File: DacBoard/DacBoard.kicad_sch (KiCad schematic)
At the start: 1 part

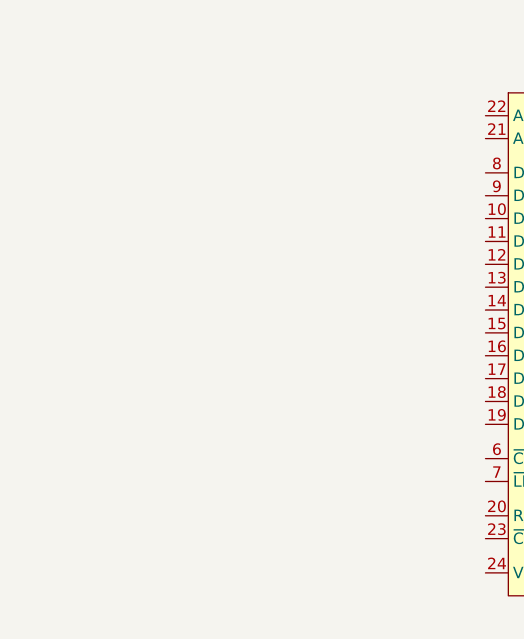
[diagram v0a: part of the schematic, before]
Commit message: Added a DAC board connector (PCIe 1x)
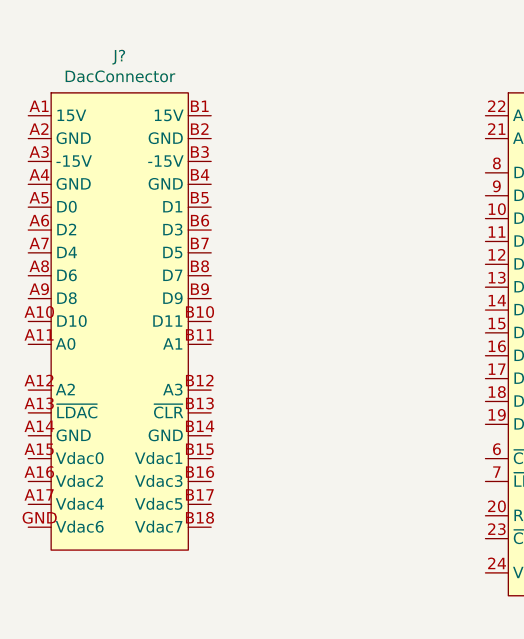
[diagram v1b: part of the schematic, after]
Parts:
- added J?: DacConnector, symbol Unichip:DacConnector
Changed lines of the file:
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@@
 (kicad_sch (version 20210126) (generator eeschema)
   (paper "A4")
+  (symbol (lib_id "Unichip:DacConnector") (at 86.36 50.8 0) (unit 1)
+    (in_bom yes) (on_board yes)
+    (property "Reference" "J?" (id 0) (at 86.36 46.7163 0))
+    (property "Value" "DacConnector" (id 1) (at 86.36 49.015 0))
+    (property "Footprint" "" (id 2) (at 86.36 50.8 0)
+      (effects (font (size 1.27 1.27)) hide)
+    )
+    (property "Datasheet" "" (id 3) (at 86.36 50.8 0)
+      (effects (font (size 1.27 1.27)) hide)
+    )
+    (pin "A1")
+    (pin "A2")
+    (pin "A3")
+    (pin "B1")
+    (pin "B2")
+    (pin "B3")
+    (pin "A4")
+    (pin "A5")
+    (pin "A6")
+    (pin "A7")
+    (pin "A8")
+    (pin "A9")
+    (pin "A10")
+    (pin "A11")
+    (pin "B6")
+    (pin "B7")
+    (pin "B8")
+    (pin "B9")
+    (pin "B10")
+    (pin "B11")
+    (pin "B4")
+    (pin "A12")
+    (pin "A13")
+    (pin "A14")
+    (pin "A15")
+    (pin "A16")
+    (pin "A17")
+    (pin "GND")
+    (pin "B12")
+    (pin "B14")
+    (pin "B15")
+    (pin "B13")
+    (pin "B16")
+    (pin "B17")
+    (pin "B18")
+    (pin "B5")
+  )
   (symbol (lib_id "Unichip:AD5725") (at 137.16 50.8 0) (unit 1)
     (in_bom yes) (on_board yes)
@@
   )
   (symbol_instances
+    (path "/40e80e6f-12f5-4eec-bb61-d86ec9cd78fd"
+      (reference "J?") (unit 1) (value "DacConnector") (footprint "")
+    )
     (path "/86d8534c-a77c-4bf0-ac2d-81d422c9a516"
       (reference "U?") (unit 1) (value "AD5725") (footprint "")

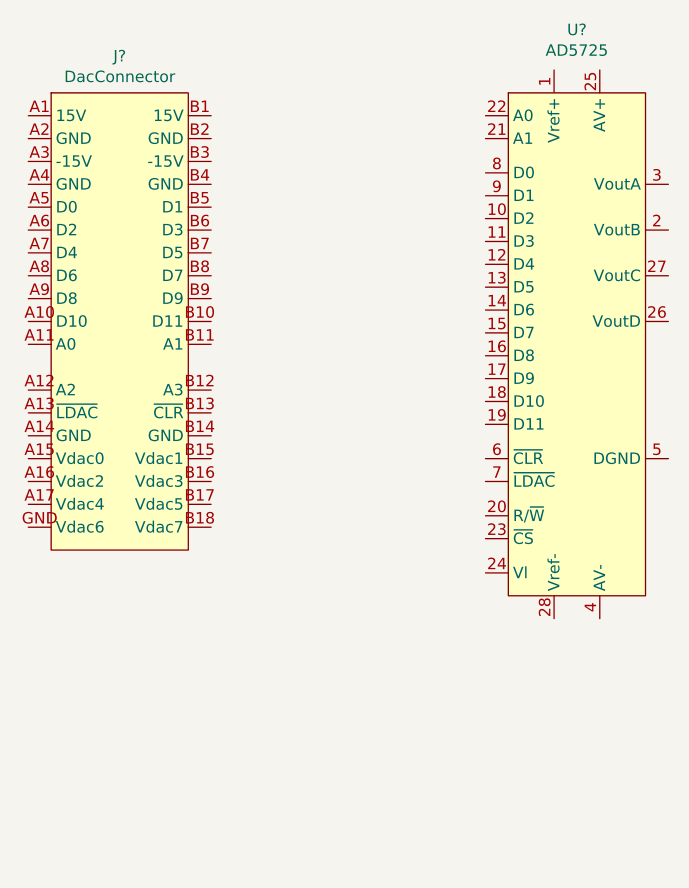
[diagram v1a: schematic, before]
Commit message: Changed DacConnector to be PCIe 4x
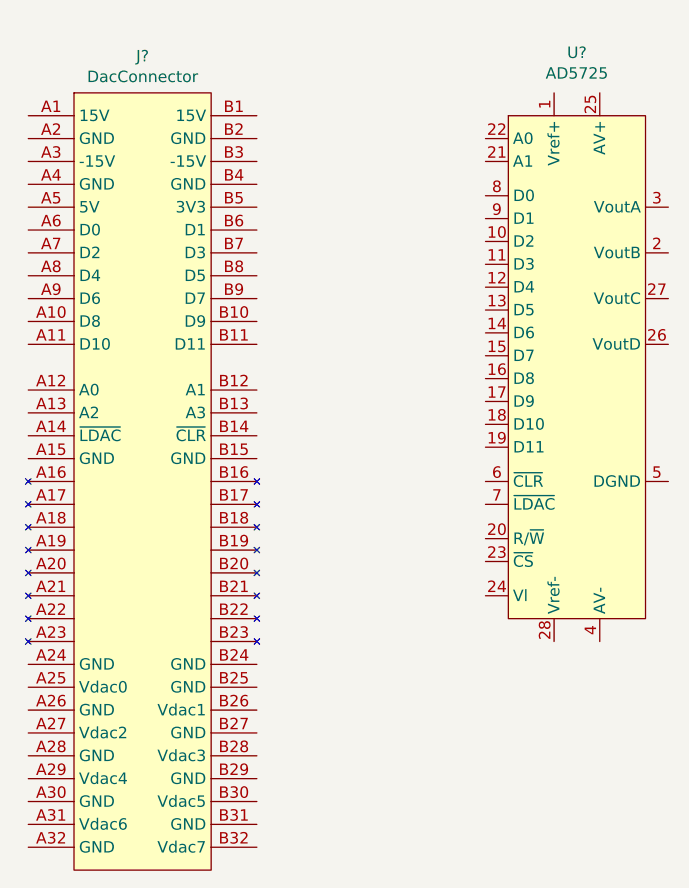
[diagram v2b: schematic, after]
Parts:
- J?: footprint (none) -> Connector_PCBEdge:BUS_PCIexpress_x4
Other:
- company: (none) -> Cole Johnson
- title: (none) -> Unichip DAC Board
- moved on the sheet: U?
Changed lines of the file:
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@@
 (kicad_sch (version 20210126) (generator eeschema)
-  (paper "A4")
-  (symbol (lib_id "Unichip:DacConnector") (at 86.36 50.8 0) (unit 1)
+  (paper "USLetter")
+  (title_block
+    (title "Unichip DAC Board")
+    (rev "A")
+    (company "Cole Johnson")
+  )
+  (symbol (lib_id "Unichip:AD5725") (at 137.16 53.34 0) (unit 1)
     (in_bom yes) (on_board yes)
-    (property "Reference" "J?" (id 0) (at 86.36 46.7163 0))
-    (property "Value" "DacConnector" (id 1) (at 86.36 49.015 0))
-    (property "Footprint" "" (id 2) (at 86.36 50.8 0)
+    (property "Reference" "U?" (id 0) (at 137.16 46.3358 0))
+    (property "Value" "AD5725" (id 1) (at 137.16 48.6345 0))
+    (property "Footprint" "" (id 2) (at 127 80.01 0)
       (effects (font (size 1.27 1.27)) hide)
     )
-    (property "Datasheet" "" (id 3) (at 86.36 50.8 0)
-      (effects (font (size 1.27 1.27)) hide)
-    )
-    (pin "A1")
-    (pin "A2")
-    (pin "A3")
-    (pin "B1")
-    (pin "B2")
-    (pin "B3")
-    (pin "A4")
-    (pin "A5")
-    (pin "A6")
-    (pin "A7")
-    (pin "A8")
-    (pin "A9")
-    (pin "A10")
-    (pin "A11")
-    (pin "B6")
-    (pin "B7")
-    (pin "B8")
-    (pin "B9")
-    (pin "B10")
-    (pin "B11")
-    (pin "B4")
-    (pin "A12")
-    (pin "A13")
-    (pin "A14")
-    (pin "A15")
-    (pin "A16")
-    (pin "A17")
-    (pin "GND")
-    (pin "B12")
-    (pin "B14")
-    (pin "B15")
-    (pin "B13")
-    (pin "B16")
-    (pin "B17")
-    (pin "B18")
-    (pin "B5")
-  )
-  (symbol (lib_id "Unichip:AD5725") (at 137.16 50.8 0) (unit 1)
-    (in_bom yes) (on_board yes)
-    (property "Reference" "U?" (id 0) (at 137.16 43.7958 0))
-    (property "Value" "AD5725" (id 1) (at 137.16 46.0945 0))
-    (property "Footprint" "" (id 2) (at 127 77.47 0)
-      (effects (font (size 1.27 1.27)) hide)
-    )
-    (property "Datasheet" "" (id 3) (at 127 77.47 0)
+    (property "Datasheet" "" (id 3) (at 127 80.01 0)
       (effects (font (size 1.27 1.27)) hide)
     )
@@
     (pin "28")
   )
+  (symbol (lib_id "Unichip:DacConnector") (at 88.9 50.8 0) (unit 1)
+    (in_bom yes) (on_board yes)
+    (property "Reference" "J?" (id 0) (at 88.9 46.7163 0))
+    (property "Value" "DacConnector" (id 1) (at 88.9 49.015 0))
+    (property "Footprint" "Connector_PCBEdge:BUS_PCIexpress_x4" (id 2) (at 88.9 50.8 0)
+      (effects (font (size 1.27 1.27)) hide)
+    )
+    (property "Datasheet" "" (id 3) (at 88.9 50.8 0)
+      (effects (font (size 1.27 1.27)) hide)
+    )
+    (pin "A1")
+    (pin "A2")
+    (pin "A3")
+    (pin "B1")
+    (pin "B2")
+    (pin "B3")
+    (pin "A4")
+    (pin "A5")
+    (pin "A6")
+    (pin "A7")
+    (pin "A8")
+    (pin "A9")
+    (pin "A10")
+    (pin "A11")
+    (pin "B6")
+    (pin "B7")
+    (pin "B8")
+    (pin "B9")
+    (pin "B10")
+    (pin "B11")
+    (pin "B4")
+    (pin "A12")
+    (pin "A13")
+    (pin "A14")
+    (pin "A15")
+    (pin "A16")
+    (pin "A17")
+    (pin "A18")
+    (pin "B12")
+    (pin "B14")
+    (pin "B15")
+    (pin "B13")
+    (pin "B16")
+    (pin "B17")
+    (pin "B18")
+    (pin "B5")
+    (pin "B32")
+    (pin "B31")
+    (pin "B30")
+    (pin "B29")
+    (pin "B28")
+    (pin "B27")
+    (pin "B26")
+    (pin "B25")
+    (pin "B24")
+    (pin "A24")
+    (pin "A25")
+    (pin "A26")
+    (pin "A27")
+    (pin "A28")
+    (pin "A29")
+    (pin "A30")
+    (pin "A31")
+    (pin "A32")
+    (pin "A19")
+    (pin "A20")
+    (pin "A21")
+    (pin "A22")
+    (pin "A23")
+    (pin "B23")
+    (pin "B22")
+    (pin "B21")
+    (pin "B20")
+    (pin "B19")
+  )
   (sheet_instances
     (path "/" (page "1"))
@@
   (symbol_instances
     (path "/40e80e6f-12f5-4eec-bb61-d86ec9cd78fd"
-      (reference "J?") (unit 1) (value "DacConnector") (footprint "")
+      (reference "J?") (unit 1) (value "DacConnector") (footprint "Connector_PCBEdge:BUS_PCIexpress_x4")
     )
     (path "/86d8534c-a77c-4bf0-ac2d-81d422c9a516"

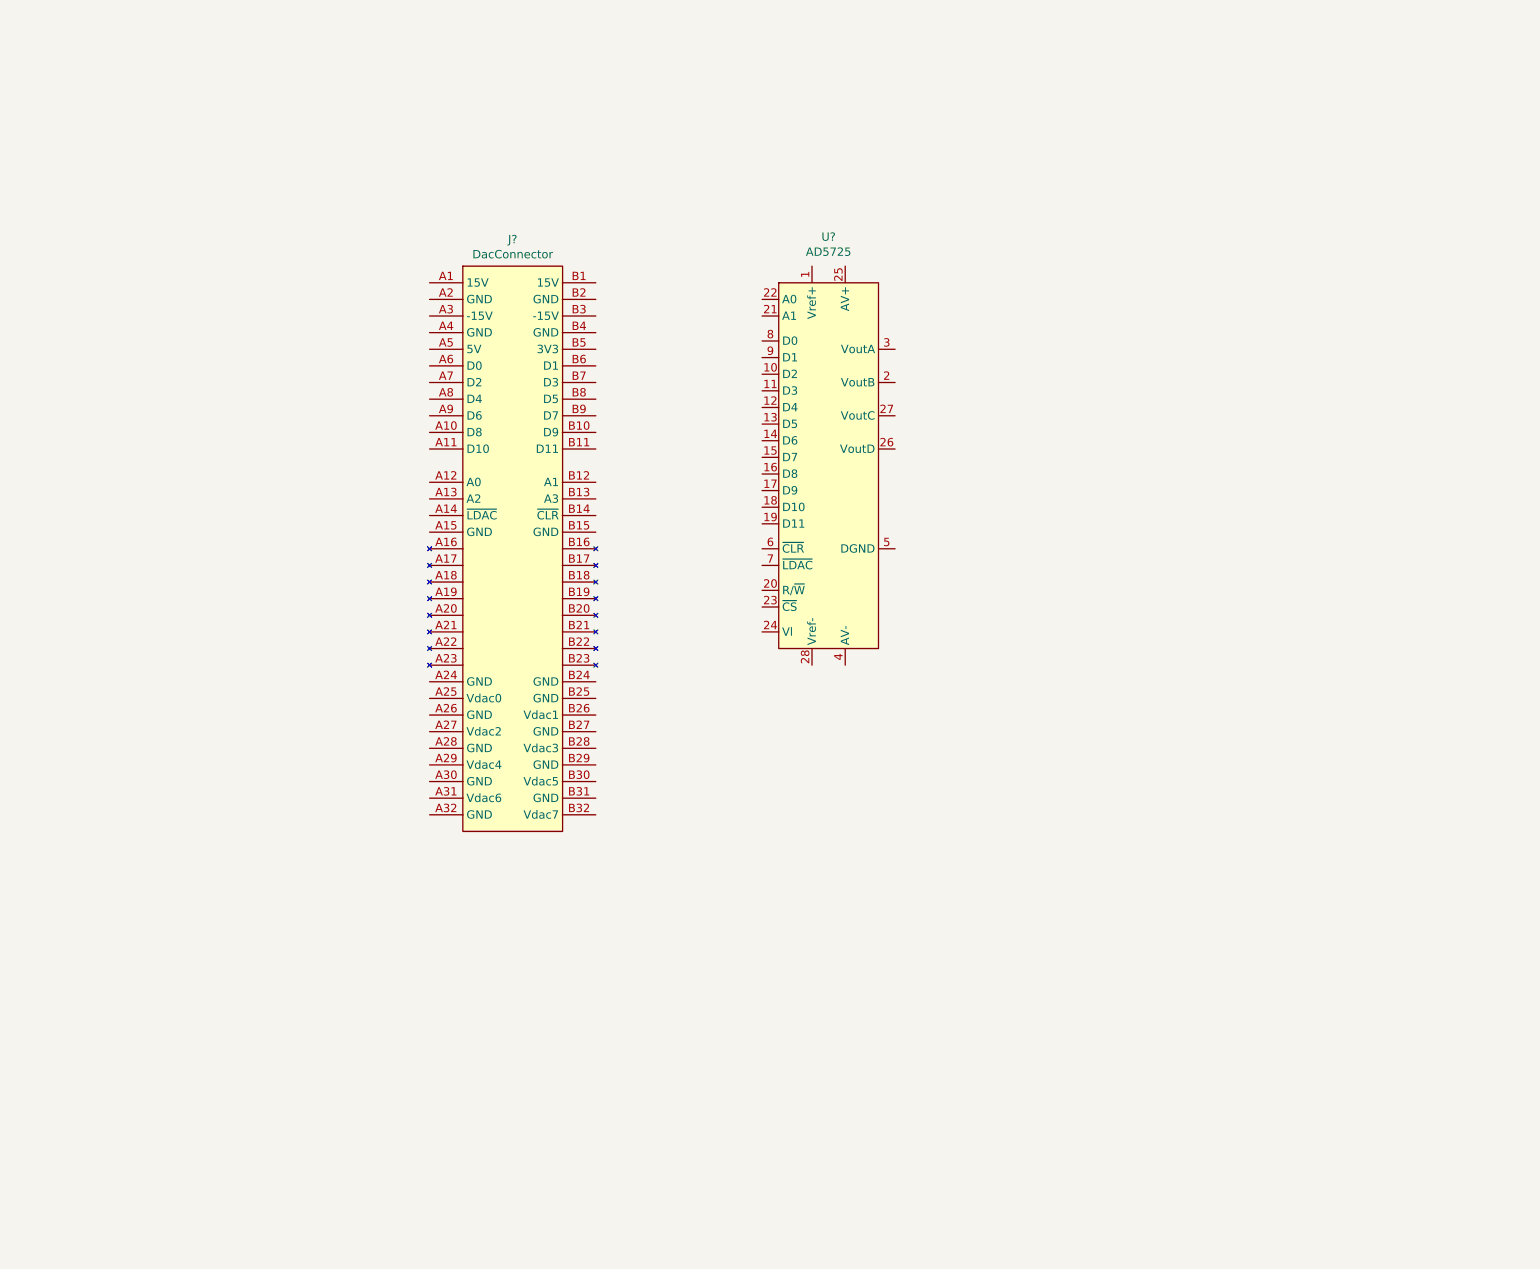
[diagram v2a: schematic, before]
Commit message: Added AD688 and filled in schematic (ERC needs testing)
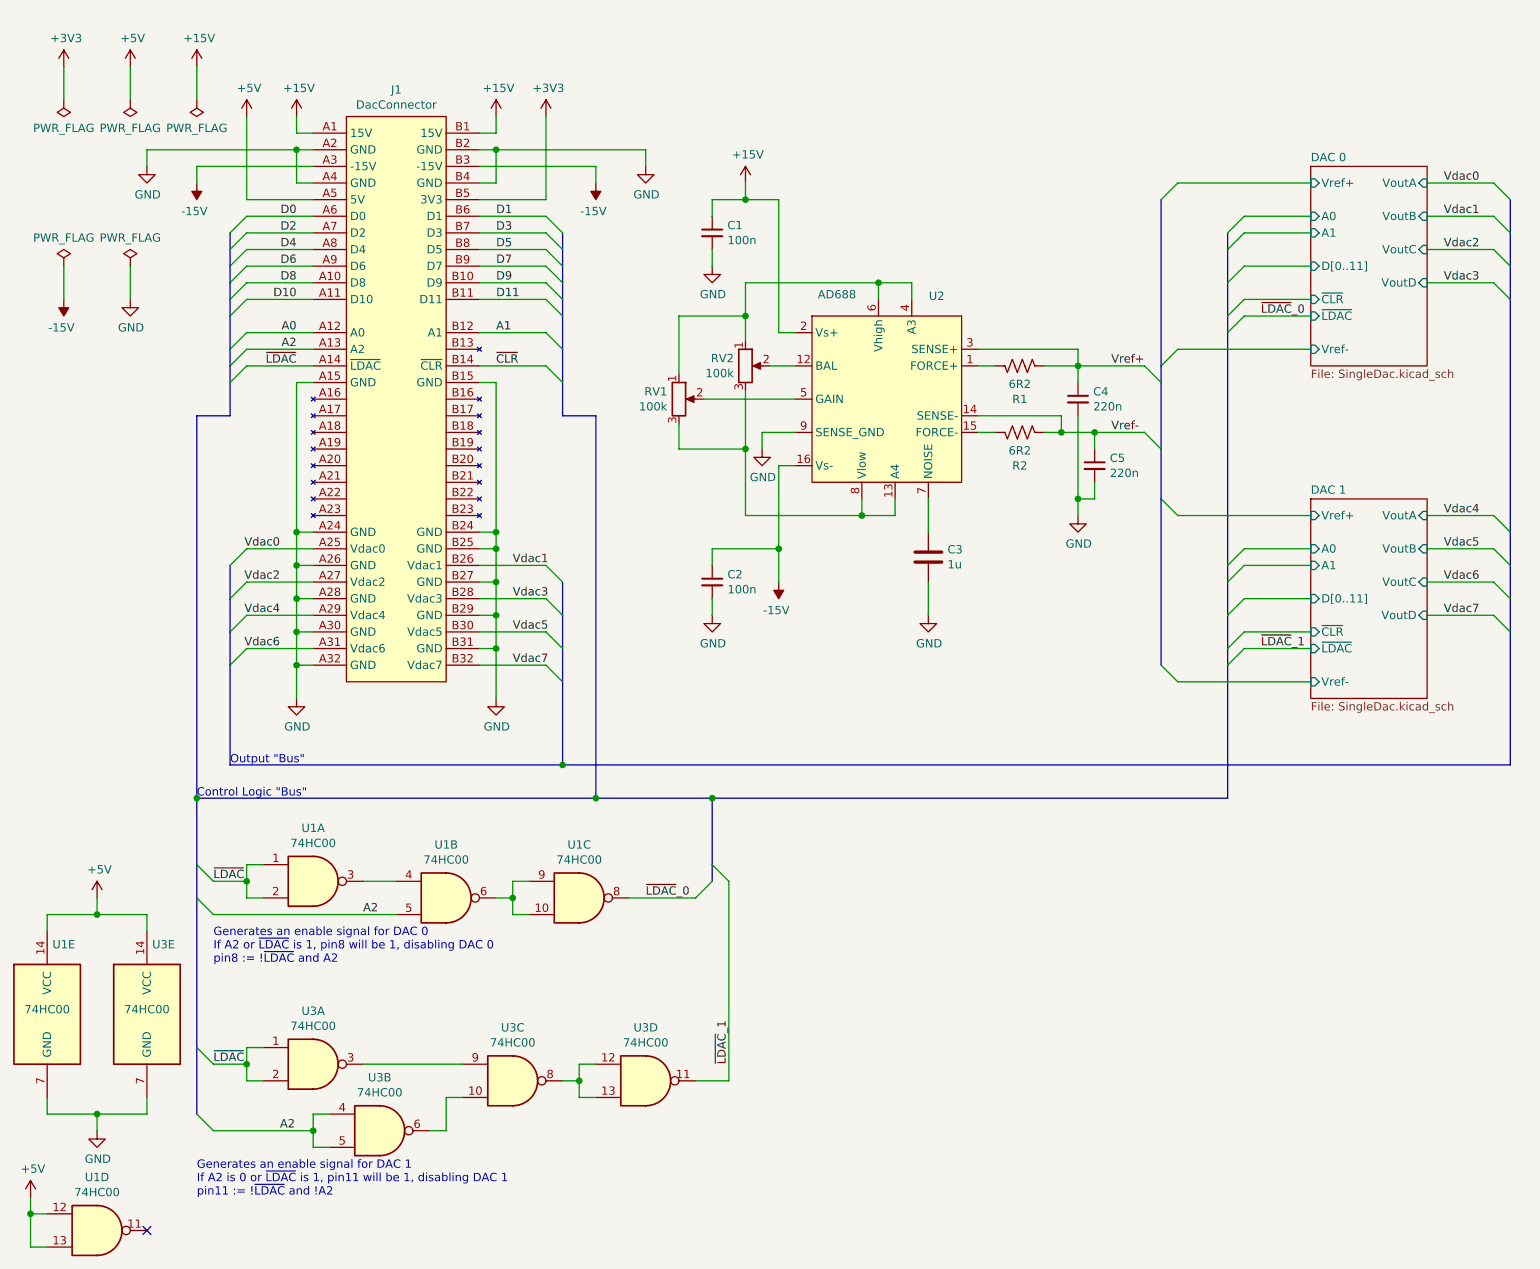
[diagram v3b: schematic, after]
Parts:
- removed U?: AD5725, symbol Unichip:AD5725
- added C1, C2: 100n, symbol Device:C_Small
- added C3: 1u, symbol Device:C
- added C4, C5: 220n, symbol Device:C_Small
- added R1, R2: 6R2, symbol Device:R_US
- added RV1, RV2: 100k, symbol Device:R_POT
- added U1, U3: 74HC00, symbol 74xx:74HC00
- added U2: AD688, symbol Unichip:AD688
- gave numbers to parts that had none: 1
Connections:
- net +15V: now reaches J1.A1 (15V)
- net +15V: now also J1.B1 (15V), C1.1, U2.2 (Vs+)
- net D8: now reaches J1.A10 (D8)
- net D10: now reaches J1.A11 (D10)
- net A0: now reaches J1.A12 (A0)
- net A2: now reaches J1.A13 (A2)
- net A2: now also U1.5, U3.4, U3.5
- net ~LDAC: now reaches J1.A14 (~LDAC)
- net ~LDAC: now also U1.1, U1.2, U3.1, U3.2
- net GND: now reaches J1.A15 (GND)
- net GND: now also J1.A2 (GND), J1.A24 (GND), J1.A26 (GND), J1.A28 (GND), J1.A30 (GND), J1.A32 (GND), J1.A4 (GND), J1.B15 (GND), J1.B2 (GND), J1.B24 (GND), J1.B25 (GND), J1.B27 (GND), J1.B29 (GND), J1.B31 (GND), J1.B4 (GND), C1.2, C2.2, C3.2, C4.2, C5.2, U1.7 (GND), U2.9 (SENSE_GND), U3.7 (GND)
- net Vdac0: now reaches J1.A25 (Vdac0)
- net Vdac2: now reaches J1.A27 (Vdac2)
- net Vdac4: now reaches J1.A29 (Vdac4)
- net -15V: now reaches J1.A3 (-15V)
- net -15V: now also J1.B3 (-15V), C2.1, U2.16 (Vs-)
- net Vdac6: now reaches J1.A31 (Vdac6)
- net +5V: now reaches J1.A5 (5V)
- net +5V: now also U1.12, U1.13, U1.14 (VCC), U3.14 (VCC)
- net D0: now reaches J1.A6 (D0)
- net D2: now reaches J1.A7 (D2)
- net D4: now reaches J1.A8 (D4)
- net D6: now reaches J1.A9 (D6)
- net D9: now reaches J1.B10 (D9)
- net D11: now reaches J1.B11 (D11)
- net A1: now reaches J1.B12 (A1)
- net ~CLR: now reaches J1.B14 (~CLR)
- net Vdac1: now reaches J1.B26 (Vdac1)
- net Vdac3: now reaches J1.B28 (Vdac3)
- net Vdac5: now reaches J1.B30 (Vdac5)
- net Vdac7: now reaches J1.B32 (Vdac7)
- net +3V3: now reaches J1.B5 (3V3)
- net D1: now reaches J1.B6 (D1)
- net D3: now reaches J1.B7 (D3)
- net D5: now reaches J1.B8 (D5)
- net D7: now reaches J1.B9 (D7)
- new net: R2.2, U2.15 (FORCE-)
- new net: C3.1, U2.7 (NOISE)
- new net: RV1.1, RV2.1, U2.4 (A3), U2.6 (Vhigh)
- new net: RV1.2, U2.5 (GAIN)
- new net: RV1.3, RV2.3, U2.13 (A4), U2.8 (Vlow)
- new net: U3.12, U3.13, U3.8
- new net: R1.2, U2.1 (FORCE+)
- new net: U3.3, U3.9
- new net: U3.10, U3.6
- new net: RV2.2, U2.12 (BAL)
- new net: U1.10, U1.6, U1.9
- new net: U1.3, U1.4
- new net Vref+: C4.1, R1.1, U2.3 (SENSE+)
- new net Vref-: C5.1, R2.1, U2.14 (SENSE-)
- new net ~LDAC~_0: U1.8
- new net ~LDAC~_1: U3.11
- no-connect marks 0 -> 1
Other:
- added sheet DAC 0 (SingleDac.kicad_sch)
- added sheet DAC 1 (SingleDac.kicad_sch)
- note added: "Control Logic "Bus""
- note added: "Generates an enable signal for DAC 0 If A2 or ~LDAC is 1, pin8 will be 1, disabling DAC 0 pin8 := !~LDAC and A2"
- note added: "Generates an enable signal for DAC 1 If A2 is 0 or ~LDAC is 1, pin11 will be 1, disabling DAC 1 pin11 := !~LDAC and !A2"
- note added: "Output "Bus""

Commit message: Changed data bus to single wires
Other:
- sheet DAC 0 ports: added D0, D1, D10, D11, D2, D3, D4, D5, D6, D7, D8, D9; removed D[0..11]
- sheet DAC 1 ports: added D0, D1, D10, D11, D2, D3, D4, D5, D6, D7, D8, D9; removed D[0..11]
